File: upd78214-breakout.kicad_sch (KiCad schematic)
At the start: 5 parts, among them U1 upd78214-64p-qfp, U2 tmp87c800df, X1 USB-B1HSB6

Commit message: Prog pins labelled
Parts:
- gave numbers to parts that had none: 2
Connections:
- net ~{PROG_OE}: now reaches U1.1 (p6,4/~{RD})
- net PROG_A14: now reaches U1.11 (p5,6/a14)
- net PROG_A13: now reaches U1.12 (p5,5/a13)
- net PROG_A12: now reaches U1.13 (p5,4/a12)
- net PROG_A11: now reaches U1.14 (p5,3/a11)
- net PROG_A10: now reaches U1.15 (p5,2/a10)
- net PROG_A9: now reaches U1.16 (p5,1/a9)
- net PROG_A8: now reaches U1.17 (p5,0/a8)
- net PROG_D7: now reaches U1.18 (p4,7/ad7)
- net PROG_D6: now reaches U1.19 (p4,6/ad6)
- net PROG_D5: now reaches U1.20 (p4,5/ad5)
- net PROG_D4: now reaches U1.21 (p4,4/ad4)
- net PROG_D3: now reaches U1.22 (p4,3/ad3)
- net PROG_D2: now reaches U1.23 (p4,2/ad2)
- net PROG_D1: now reaches U1.25 (p4,1/ad1)
- net PROG_D0: now reaches U1.26 (p4,0/ad0)
- net PROG_Vpp: now reaches U1.40 (~{EA})
- net PROG_A0: now reaches U1.54 (p0,0)
- net PROG_A1: now reaches U1.55 (p0,1)
- net PROG_A2: now reaches U1.56 (p0,2)
- net PROG_A3: now reaches U1.57 (p0,3)
- net PROG_A4: now reaches U1.58 (p0,4)
- net PROG_A5: now reaches U1.59 (p0,5)
- net ~{PROG_RESET}: now reaches U1.6 (~{RESET})
- net PROG_A6: now reaches U1.60 (p0,6)
- net PROG_A7: now reaches U1.61 (p0,7)
- net ~{PROG_CE}: now reaches U1.64 (p6,5/~{WR})
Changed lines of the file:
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@@
   (no_connect (at 27.305 27.94))
   (no_connect (at 27.305 30.48))
+  (wire (pts (xy 103.505 48.26) (xy 111.125 48.26))
+    (stroke (width 0) (type default) (color 0 0 0 0))
+  )
   (wire (pts (xy 92.075 189.23) (xy 92.075 192.405))
     (stroke (width 0) (type default) (color 0 0 0 0))
@@
     (stroke (width 0) (type default) (color 0 0 0 0))
   )
+  (wire (pts (xy 103.505 40.64) (xy 111.125 40.64))
+    (stroke (width 0) (type default) (color 0 0 0 0))
+  )
+  (wire (pts (xy 103.505 124.46) (xy 111.125 124.46))
+    (stroke (width 0) (type default) (color 0 0 0 0))
+  )
   (wire (pts (xy 41.275 33.02) (xy 34.925 33.02))
     (stroke (width 0) (type default) (color 0 0 0 0))
   )
+  (wire (pts (xy 103.505 127) (xy 111.125 127))
+    (stroke (width 0) (type default) (color 0 0 0 0))
+  )
+  (wire (pts (xy 73.025 43.18) (xy 78.105 43.18))
+    (stroke (width 0) (type default) (color 0 0 0 0))
+  )
+  (wire (pts (xy 103.505 121.92) (xy 111.125 121.92))
+    (stroke (width 0) (type default) (color 0 0 0 0))
+  )
+  (wire (pts (xy 103.505 102.87) (xy 111.125 102.87))
+    (stroke (width 0) (type default) (color 0 0 0 0))
+  )
   (wire (pts (xy 157.48 191.77) (xy 165.1 191.77))
     (stroke (width 0) (type default) (color 0 0 0 0))
   )
+  (wire (pts (xy 103.505 156.21) (xy 111.125 156.21))
+    (stroke (width 0) (type default) (color 0 0 0 0))
+  )
   (wire (pts (xy 86.995 20.32) (xy 86.995 22.86))
     (stroke (width 0) (type default) (color 0 0 0 0))
   )
+  (wire (pts (xy 103.505 53.34) (xy 111.125 53.34))
+    (stroke (width 0) (type default) (color 0 0 0 0))
+  )
   (wire (pts (xy 34.925 33.02) (xy 27.305 33.02))
     (stroke (width 0) (type default) (color 0 0 0 0))
   )
+  (wire (pts (xy 103.505 38.1) (xy 111.125 38.1))
+    (stroke (width 0) (type default) (color 0 0 0 0))
+  )
+  (wire (pts (xy 103.505 118.11) (xy 111.125 118.11))
+    (stroke (width 0) (type default) (color 0 0 0 0))
+  )
+  (wire (pts (xy 103.505 137.16) (xy 111.125 137.16))
+    (stroke (width 0) (type default) (color 0 0 0 0))
+  )
   (wire (pts (xy 81.28 20.32) (xy 86.995 20.32))
     (stroke (width 0) (type default) (color 0 0 0 0))
@@
     (stroke (width 0) (type default) (color 0 0 0 0))
   )
+  (wire (pts (xy 103.505 129.54) (xy 111.125 129.54))
+    (stroke (width 0) (type default) (color 0 0 0 0))
+  )
+  (wire (pts (xy 103.505 105.41) (xy 111.125 105.41))
+    (stroke (width 0) (type default) (color 0 0 0 0))
+  )
   (wire (pts (xy 165.1 191.77) (xy 165.1 187.96))
     (stroke (width 0) (type default) (color 0 0 0 0))
   )
+  (wire (pts (xy 103.505 43.18) (xy 111.125 43.18))
+    (stroke (width 0) (type default) (color 0 0 0 0))
+  )
   (wire (pts (xy 156.845 20.955) (xy 165.1 20.955))
     (stroke (width 0) (type default) (color 0 0 0 0))
@@
     (stroke (width 0) (type default) (color 0 0 0 0))
   )
+  (wire (pts (xy 103.505 45.72) (xy 111.125 45.72))
+    (stroke (width 0) (type default) (color 0 0 0 0))
+  )
   (wire (pts (xy 94.615 189.23) (xy 94.615 192.405))
     (stroke (width 0) (type default) (color 0 0 0 0))
   )
+  (wire (pts (xy 103.505 132.08) (xy 111.125 132.08))
+    (stroke (width 0) (type default) (color 0 0 0 0))
+  )
   (wire (pts (xy 34.925 25.4) (xy 41.275 25.4))
     (stroke (width 0) (type default) (color 0 0 0 0))
   )
+  (wire (pts (xy 103.505 100.33) (xy 111.125 100.33))
+    (stroke (width 0) (type default) (color 0 0 0 0))
+  )
+  (wire (pts (xy 103.505 50.8) (xy 111.125 50.8))
+    (stroke (width 0) (type default) (color 0 0 0 0))
+  )
+  (wire (pts (xy 103.505 134.62) (xy 111.125 134.62))
+    (stroke (width 0) (type default) (color 0 0 0 0))
+  )
   (wire (pts (xy 156.845 18.415) (xy 156.845 20.955))
     (stroke (width 0) (type default) (color 0 0 0 0))
   )
+  (wire (pts (xy 103.505 113.03) (xy 111.125 113.03))
+    (stroke (width 0) (type default) (color 0 0 0 0))
+  )
+  (wire (pts (xy 103.505 107.95) (xy 111.125 107.95))
+    (stroke (width 0) (type default) (color 0 0 0 0))
+  )
+  (wire (pts (xy 73.025 35.56) (xy 78.105 35.56))
+    (stroke (width 0) (type default) (color 0 0 0 0))
+  )
   (wire (pts (xy 92.075 192.405) (xy 89.535 192.405))
     (stroke (width 0) (type default) (color 0 0 0 0))
@@
     (stroke (width 0) (type default) (color 0 0 0 0))
   )
+  (wire (pts (xy 103.505 110.49) (xy 111.125 110.49))
+    (stroke (width 0) (type default) (color 0 0 0 0))
+  )
   (wire (pts (xy 34.925 25.4) (xy 27.305 25.4))
     (stroke (width 0) (type default) (color 0 0 0 0))
   )
+  (wire (pts (xy 103.505 115.57) (xy 111.125 115.57))
+    (stroke (width 0) (type default) (color 0 0 0 0))
+  )
   (wire (pts (xy 89.535 192.405) (xy 85.09 192.405))
     (stroke (width 0) (type default) (color 0 0 0 0))
+  )
+  (wire (pts (xy 103.505 35.56) (xy 111.125 35.56))
+    (stroke (width 0) (type default) (color 0 0 0 0))
+  )
+  (wire (pts (xy 103.505 153.67) (xy 111.125 153.67))
+    (stroke (width 0) (type default) (color 0 0 0 0))
+  )
+  (label "PROG_A0" (at 111.125 35.56 0)
+    (effects (font (size 1.27 1.27)) (justify left bottom))
+  )
+  (label "PROG_A7" (at 111.125 53.34 0)
+    (effects (font (size 1.27 1.27)) (justify left bottom))
+  )
+  (label "PROG_D7" (at 111.125 118.11 0)
+    (effects (font (size 1.27 1.27)) (justify left bottom))
+  )
+  (label "PROG_A9" (at 111.125 124.46 0)
+    (effects (font (size 1.27 1.27)) (justify left bottom))
+  )
+  (label "PROG_Vpp" (at 73.025 43.18 180)
+    (effects (font (size 1.27 1.27)) (justify right bottom))
+  )
+  (label "~{PROG_CE}" (at 111.125 156.21 0)
+    (effects (font (size 1.27 1.27)) (justify left bottom))
+  )
+  (label "PROG_A2" (at 111.125 40.64 0)
+    (effects (font (size 1.27 1.27)) (justify left bottom))
+  )
+  (label "~{PROG_OE}" (at 111.125 153.67 0)
+    (effects (font (size 1.27 1.27)) (justify left bottom))
+  )
+  (label "PROG_A11" (at 111.125 129.54 0)
+    (effects (font (size 1.27 1.27)) (justify left bottom))
+  )
+  (label "PROG_D6" (at 111.125 115.57 0)
+    (effects (font (size 1.27 1.27)) (justify left bottom))
+  )
+  (label "~{PROG_RESET}" (at 73.025 35.56 180)
+    (effects (font (size 1.27 1.27)) (justify right bottom))
+  )
+  (label "PROG_D5" (at 111.125 113.03 0)
+    (effects (font (size 1.27 1.27)) (justify left bottom))
+  )
+  (label "PROG_A13" (at 111.125 134.62 0)
+    (effects (font (size 1.27 1.27)) (justify left bottom))
+  )
+  (label "PROG_D1" (at 111.125 102.87 0)
+    (effects (font (size 1.27 1.27)) (justify left bottom))
+  )
+  (label "PROG_A5" (at 111.125 48.26 0)
+    (effects (font (size 1.27 1.27)) (justify left bottom))
+  )
+  (label "PROG_D4" (at 111.125 110.49 0)
+    (effects (font (size 1.27 1.27)) (justify left bottom))
+  )
+  (label "PROG_A12" (at 111.125 132.08 0)
+    (effects (font (size 1.27 1.27)) (justify left bottom))
+  )
+  (label "PROG_A6" (at 111.125 50.8 0)
+    (effects (font (size 1.27 1.27)) (justify left bottom))
+  )
+  (label "PROG_A1" (at 111.125 38.1 0)
+    (effects (font (size 1.27 1.27)) (justify left bottom))
+  )
+  (label "PROG_D0" (at 111.125 100.33 0)
+    (effects (font (size 1.27 1.27)) (justify left bottom))
+  )
+  (label "PROG_A8" (at 111.125 121.92 0)
+    (effects (font (size 1.27 1.27)) (justify left bottom))
+  )
+  (label "PROG_D2" (at 111.125 105.41 0)
+    (effects (font (size 1.27 1.27)) (justify left bottom))
+  )
+  (label "PROG_D3" (at 111.125 107.95 0)
+    (effects (font (size 1.27 1.27)) (justify left bottom))
+  )
+  (label "PROG_A3" (at 111.125 43.18 0)
+    (effects (font (size 1.27 1.27)) (justify left bottom))
+  )
+  (label "PROG_A4" (at 111.125 45.72 0)
+    (effects (font (size 1.27 1.27)) (justify left bottom))
+  )
+  (label "PROG_A14" (at 111.125 137.16 0)
+    (effects (font (size 1.27 1.27)) (justify left bottom))
+  )
+  (label "PROG_A10" (at 111.125 127 0)
+    (effects (font (size 1.27 1.27)) (justify left bottom))
   )
   (symbol (lib_id "USB-B1HSB6-2:USB-B1HSB6") (at 24.765 27.94 0) (mirror y) (unit 1)
@@
   (symbol (lib_id "Connector:TestPoint") (at 41.275 33.02 180) (unit 1)
     (in_bom yes) (on_board yes) (fields_autoplaced)
-    (property "Reference" "TP?" (id 0) (at 43.18 35.0519 0)
+    (property "Reference" "TP2" (id 0) (at 43.18 35.0519 0)
       (effects (font (size 1.27 1.27)) (justify right))
     )
@@
   (symbol (lib_id "Connector:TestPoint") (at 41.275 25.4 0) (unit 1)
     (in_bom yes) (on_board yes) (fields_autoplaced)
-    (property "Reference" "TP?" (id 0) (at 43.18 20.8279 0)
+    (property "Reference" "TP1" (id 0) (at 43.18 20.8279 0)
       (effects (font (size 1.27 1.27)) (justify left))
     )
@@
       (reference "#PWR0106") (unit 1) (value "GND") (footprint "")
     )
+    (path "/b3494da2-9112-497d-8dd3-ab62d10d763a"
+      (reference "TP1") (unit 1) (value "TestPoint") (footprint "TestPoint:TestPoint_Loop_D2.50mm_Drill1.0mm")
+    )
     (path "/14aad0c5-971e-4e33-9c5d-012743c51814"
-      (reference "TP?") (unit 1) (value "TestPoint") (footprint "TestPoint:TestPoint_Loop_D2.50mm_Drill1.0mm")
-    )
-    (path "/b3494da2-9112-497d-8dd3-ab62d10d763a"
-      (reference "TP?") (unit 1) (value "TestPoint") (footprint "TestPoint:TestPoint_Loop_D2.50mm_Drill1.0mm")
+      (reference "TP2") (unit 1) (value "TestPoint") (footprint "TestPoint:TestPoint_Loop_D2.50mm_Drill1.0mm")
     )
     (path "/69c7afce-fa24-4138-9624-1d45a5afe81a"

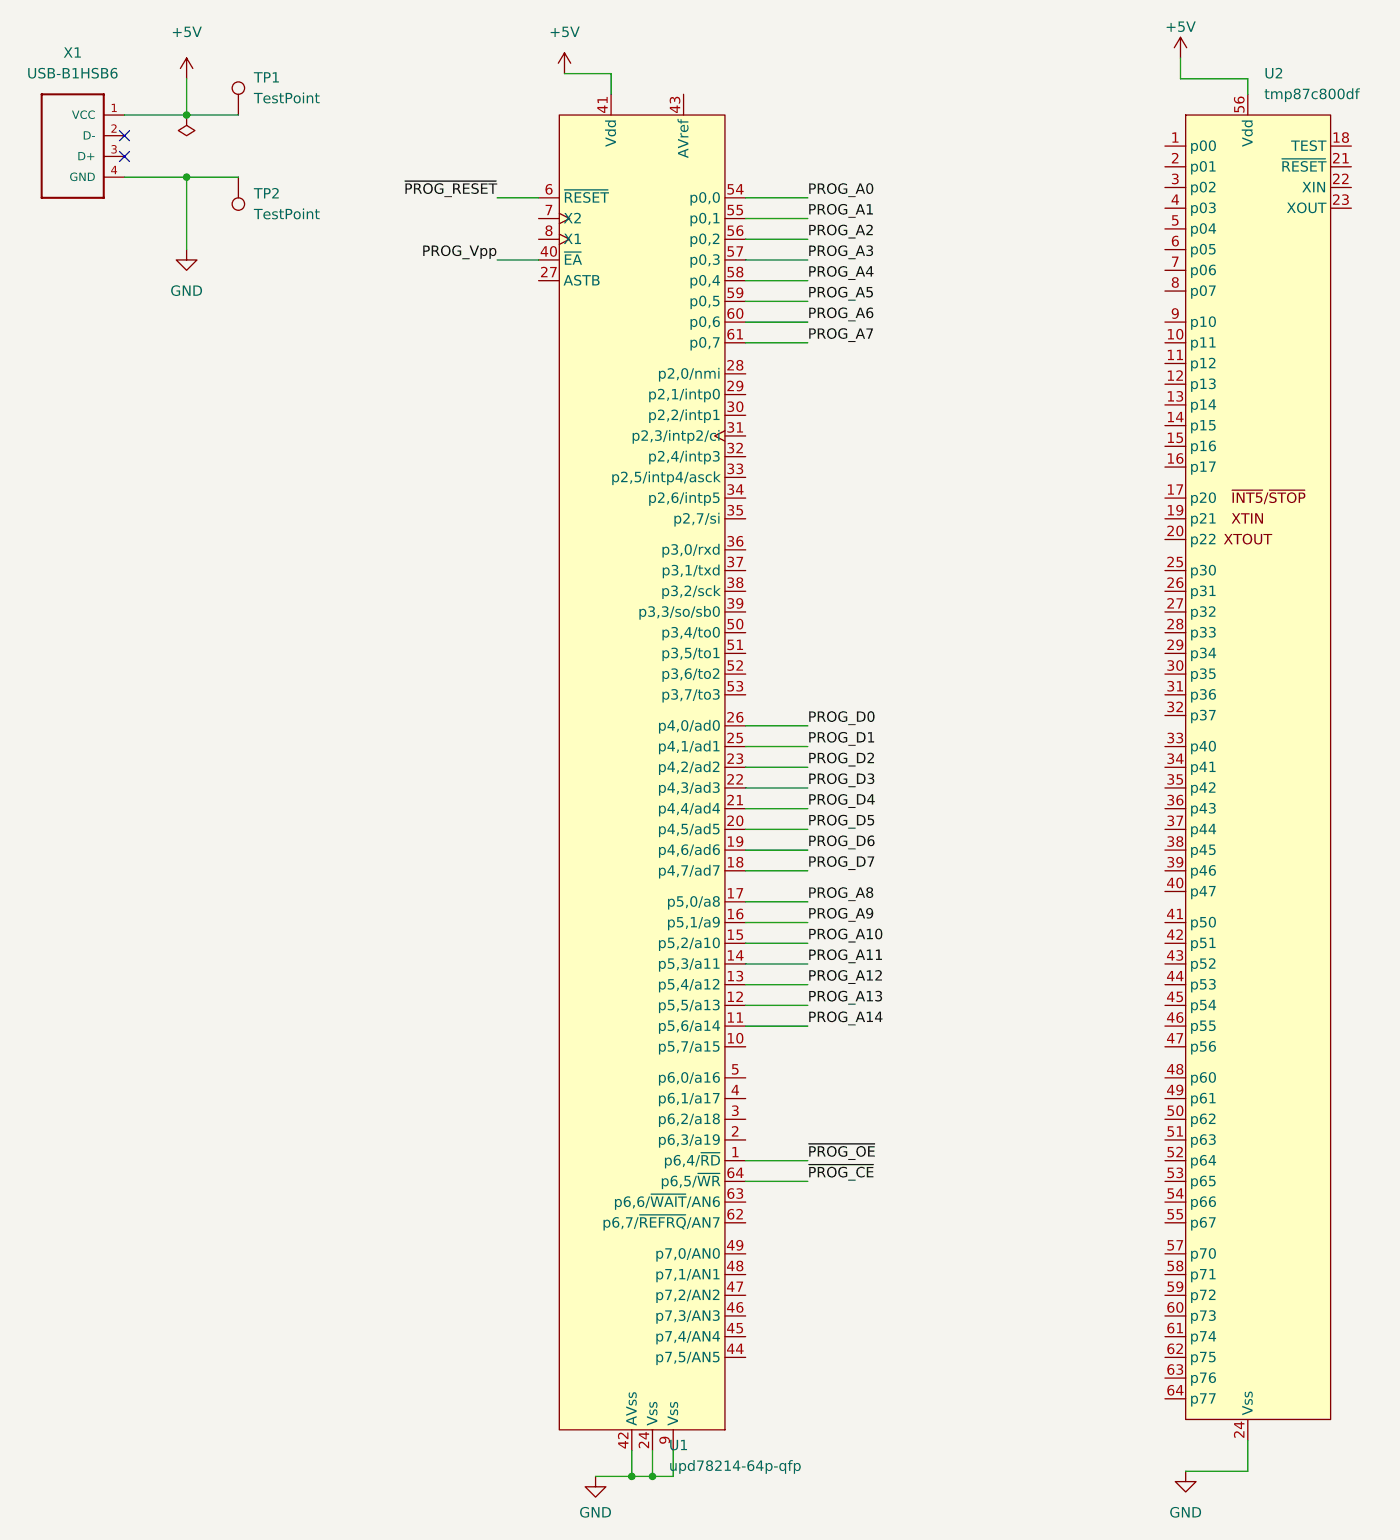
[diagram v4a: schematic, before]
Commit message: Breakout pins for NEC
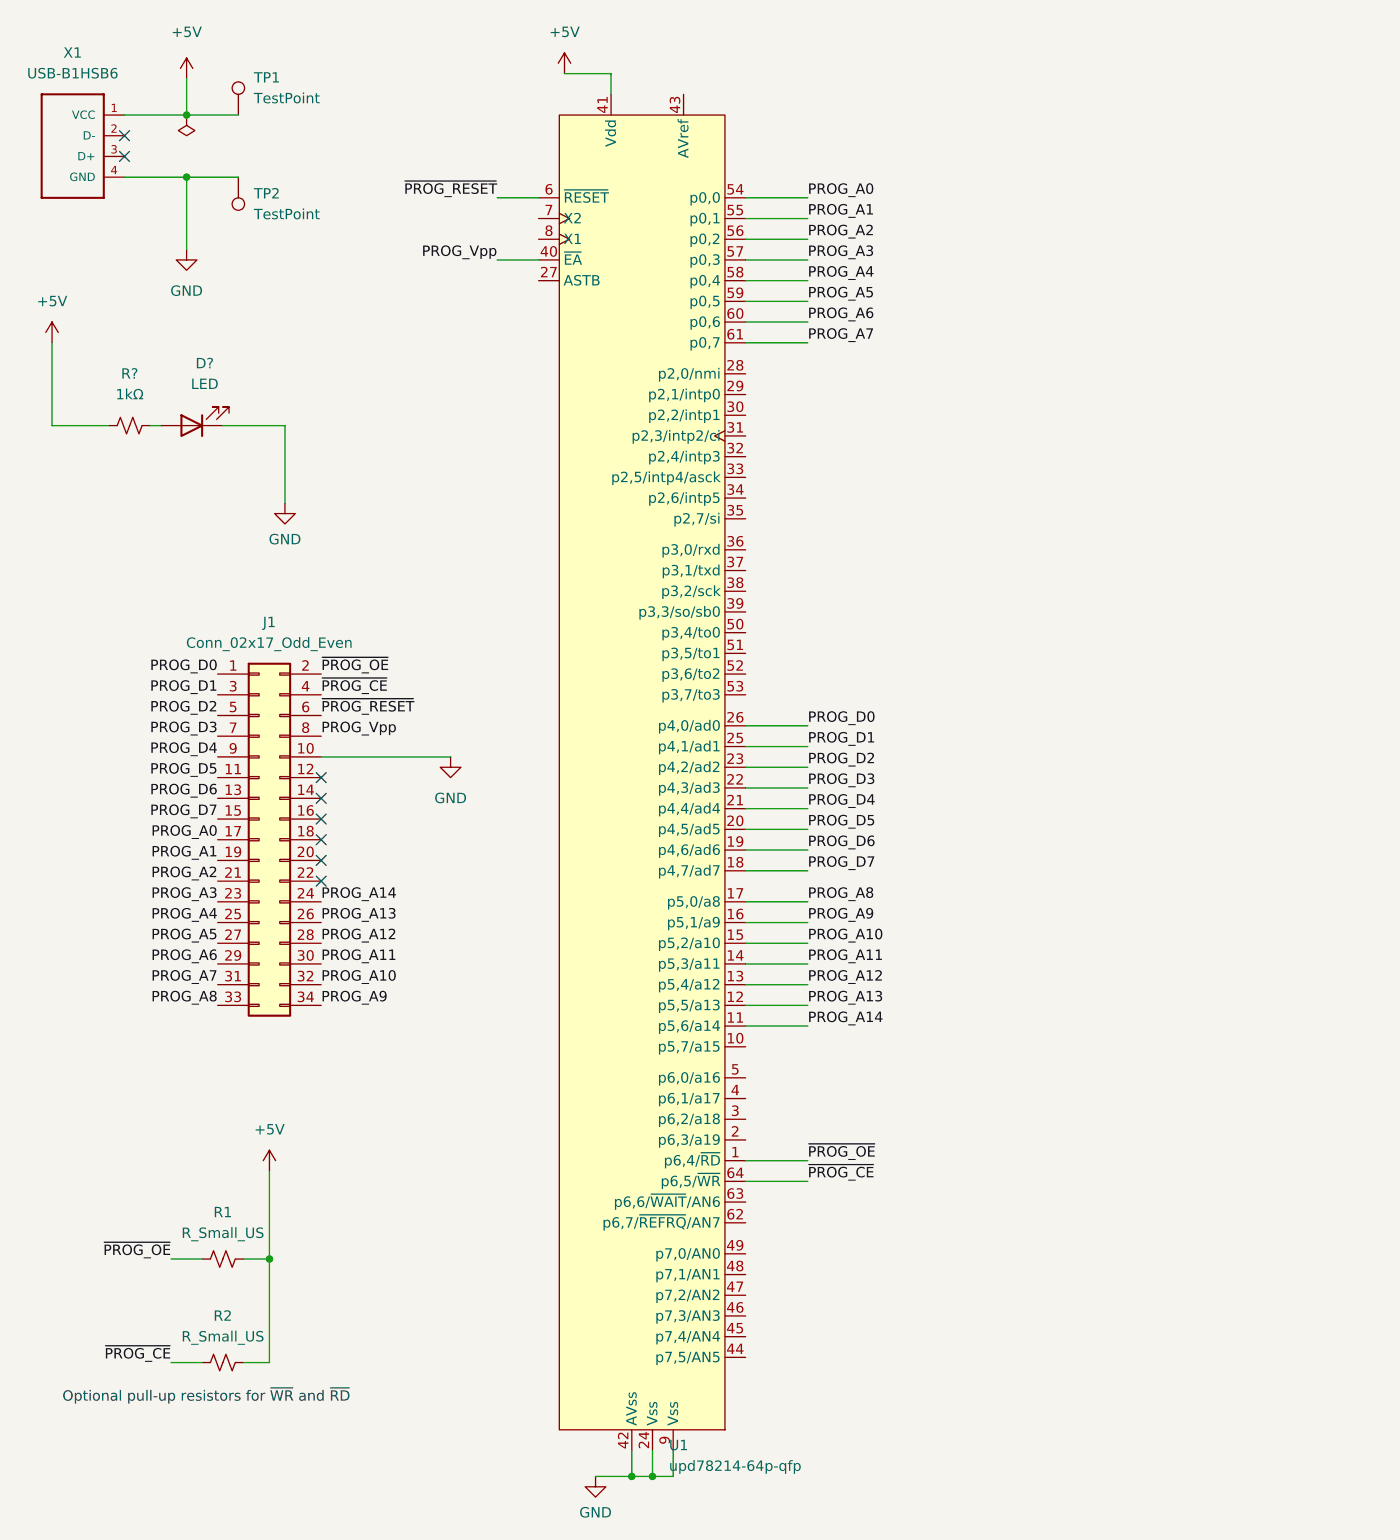
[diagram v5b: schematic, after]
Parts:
- removed U2: tmp87c800df, NEC:QFP-64_14x14_Pitch0.8mm, symbol Toshiba:tmp87c800df
- added D?: LED, LED_THT:LED_D3.0mm, symbol Device:LED
- added J1: Conn_02x17_Odd_Even, Connector_PinSocket_2.54mm:PinSocket_2x17_P2.54mm_Vertical, symbol Connector_Generic:Conn_02x17_Odd_Even
- added R1, R2: R_Small_US, Resistor_THT:R_Axial_DIN0207_L6.3mm_D2.5mm_P10.16mm_Horizontal, symbol Device:R_Small_US
- added R?: 1kΩ, Resistor_THT:R_Axial_DIN0207_L6.3mm_D2.5mm_P10.16mm_Horizontal, symbol Device:R_Small_US
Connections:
- net +5V: now also R1.2, R2.2, R?.1
- net GND: now also D?.1 (K), J1.10 (Pin_10)
- net PROG_A0: now also J1.17 (Pin_17)
- net PROG_A1: now also J1.19 (Pin_19)
- net PROG_A10: now also J1.32 (Pin_32)
- net PROG_A11: now also J1.30 (Pin_30)
- net PROG_A12: now also J1.28 (Pin_28)
- net PROG_A13: now also J1.26 (Pin_26)
- net PROG_A14: now also J1.24 (Pin_24)
- net PROG_A2: now also J1.21 (Pin_21)
- net PROG_A3: now also J1.23 (Pin_23)
- net PROG_A4: now also J1.25 (Pin_25)
- net PROG_A5: now also J1.27 (Pin_27)
- net PROG_A6: now also J1.29 (Pin_29)
- net PROG_A7: now also J1.31 (Pin_31)
- net PROG_A8: now also J1.33 (Pin_33)
- net PROG_A9: now also J1.34 (Pin_34)
- net PROG_D0: now also J1.1 (Pin_1)
- net PROG_D1: now also J1.3 (Pin_3)
- net PROG_D2: now also J1.5 (Pin_5)
- net PROG_D3: now also J1.7 (Pin_7)
- net PROG_D4: now also J1.9 (Pin_9)
- net PROG_D5: now also J1.11 (Pin_11)
- net PROG_D6: now also J1.13 (Pin_13)
- net PROG_D7: now also J1.15 (Pin_15)
- net PROG_Vpp: now also J1.8 (Pin_8)
- net ~{PROG_CE}: now also J1.4 (Pin_4), R2.1
- net ~{PROG_OE}: now also J1.2 (Pin_2), R1.1
- net ~{PROG_RESET}: now also J1.6 (Pin_6)
- new net: D?.2 (A), R?.2
- no-connect marks 2 -> 8
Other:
- note added: "Optional pull-up resistors for ~{WR} and ~{RD}"
